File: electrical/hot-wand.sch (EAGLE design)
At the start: 184 parts, among them IC1 12V R-78K12-2.0, IC2 3V3 R-78K3.3, Q1 STP19NF20, Q2 IRF510, Q3 BC846B, Q4 SIRS5800DP-T1-GE3, Q5 2N7002K, Q6 DMTH64M2LPDWQ-13, Q7 G3404, SW1 SW-TACT-SIDE, U1 TPS54560DDA, U2 1EDN8511BXUSA1, U3 INA138, U4 LM74700QDBVTQ1, U5 AP53781, U6 SSD1306-4PIN-0.91N-VERT, U7 STM32F030F4P6, Y1 27.12 MHz 10pF

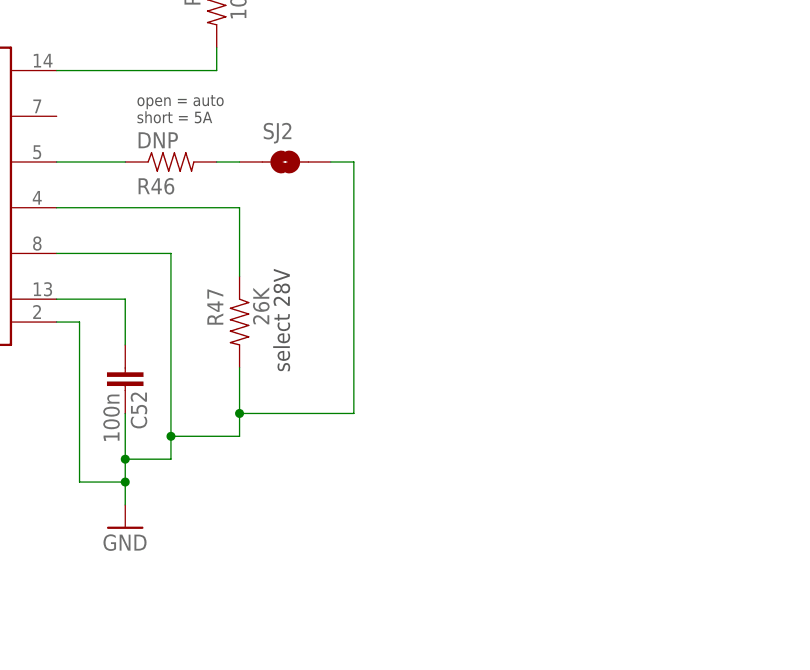
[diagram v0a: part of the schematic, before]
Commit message: added selectable voltage for USB
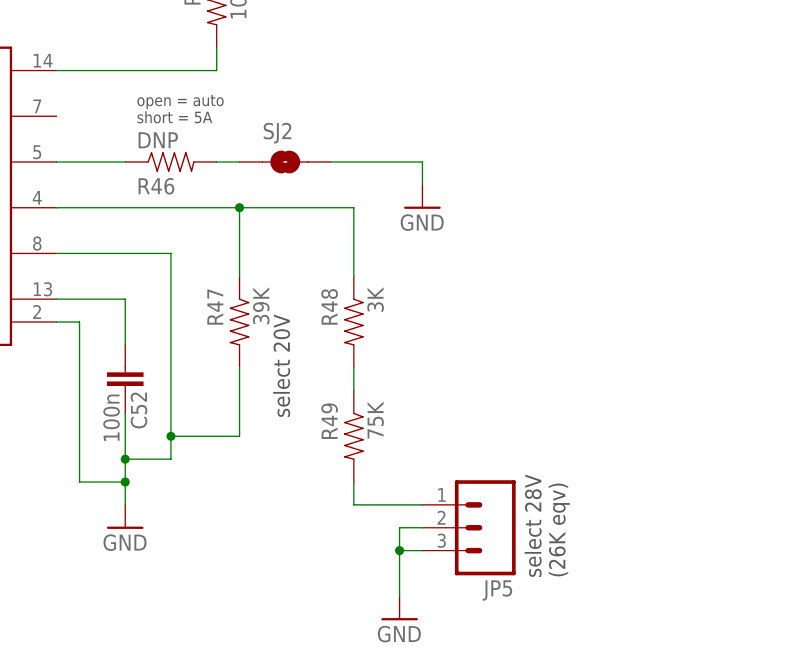
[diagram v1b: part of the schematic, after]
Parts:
- added JP5: (no value), hot-wand:M03LOCK
- added R48: 3K, hot-wand:RESISTOR0603-RES
- added R49: 75K, hot-wand:RESISTOR0603-RES
- R47: value 26K -> 39K; JLCPARTNUM C23356 -> C23153
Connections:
- new net N$60: R48.2, R49.1
- new net N$61: JP5.1, R49.2
- net GND: now also JP5.2, JP5.3
- net N$42: now also R48.1
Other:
- note added: "select 20V"
- note added: "select 28V (26K eqv)"
- note removed: "select 28V"
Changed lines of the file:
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@@
 </part>
 <part name="GND42" library="hot-wand" deviceset="GND" device=""/>
-<part name="R47" library="hot-wand" deviceset="RESISTOR" device="0603-RES" value="26K">
-<attribute name="JLCPARTNUM" value="C23356"/>
+<part name="R47" library="hot-wand" deviceset="RESISTOR" device="0603-RES" value="39K">
+<attribute name="JLCPARTNUM" value="C23153"/>
 </part>
 <part name="R34" library="hot-wand" deviceset="RESISTOR" device="0603-RES" value="4K7">
@@
 <part name="SJ6" library="hot-wand" deviceset="SJ-SMALL" device="-1206-SJ"/>
 <part name="SJ7" library="hot-wand" deviceset="SJ-SMALL" device="-1206-SJ"/>
+<part name="GND63" library="hot-wand" deviceset="GND" device=""/>
+<part name="R48" library="hot-wand" deviceset="RESISTOR" device="0603-RES" value="3K">
+<attribute name="JLCPARTNUM" value="C4211"/>
+</part>
+<part name="R49" library="hot-wand" deviceset="RESISTOR" device="0603-RES" value="75K">
+<attribute name="JLCPARTNUM" value="C23242"/>
+</part>
+<part name="JP5" library="hot-wand" deviceset="M03" device="LOCK"/>
+<part name="GND64" library="hot-wand" deviceset="GND" device=""/>
 </parts>
 <sheets>
@@
 0.11 Rdson</text>
 <text x="259.08" y="-251.46" size="1.016" layer="96" align="bottom-right">Bourns 5300-17-RC</text>
-<text x="156.21" y="-706.628" size="1.778" layer="97" rot="R270" align="bottom-right">select 28V</text>
+<text x="156.21" y="-711.708" size="1.778" layer="97" rot="R270" align="bottom-right">select 20V</text>
 <text x="58.42" y="-579.12" size="5.08" layer="97">XT-30 DC Input</text>
 <text x="25.4" y="-675.64" size="5.08" layer="97">USB-PD Input</text>
@@
 curr meas</text>
 <text x="251.46" y="-15.24" size="1.27" layer="97" align="top-left">actually about 20V</text>
+<text x="184.15" y="-729.488" size="1.778" layer="97" rot="R270" align="bottom-right">select 28V
+(26K eqv)</text>
 </plain>
 <instances>
@@
 <instance part="SJ6" gate="A" x="35.56" y="-223.52"/>
 <instance part="SJ7" gate="A" x="58.42" y="-182.88" rot="R90"/>
+<instance part="GND63" gate="1" x="172.72" y="-688.34"/>
+<instance part="R48" gate="G$1" x="165.1" y="-701.04" smashed="yes" rot="R270">
+<attribute name="NAME" x="161.5186" y="-697.23" size="1.778" layer="95" rot="R270"/>
+<attribute name="VALUE" x="166.624" y="-697.23" size="1.778" layer="96" rot="R270"/>
+<attribute name="JLCPARTNUM" x="165.1" y="-701.04" size="1.778" layer="96" rot="R270" display="off"/>
+</instance>
+<instance part="R49" gate="G$1" x="165.1" y="-713.74" smashed="yes" rot="R270">
+<attribute name="NAME" x="161.5186" y="-709.93" size="1.778" layer="95" rot="R270"/>
+<attribute name="VALUE" x="166.624" y="-709.93" size="1.778" layer="96" rot="R270"/>
+<attribute name="JLCPARTNUM" x="165.1" y="-713.74" size="1.778" layer="96" rot="R270" display="off"/>
+</instance>
+<instance part="JP5" gate="G$1" x="180.34" y="-723.9" rot="R180"/>
+<instance part="GND64" gate="1" x="170.18" y="-734.06"/>
 </instances>
 <busses>
@@
 <pinref part="R47" gate="G$1" pin="2"/>
 <wire x1="144.78" y1="-713.74" x2="152.4" y2="-713.74" width="0.1524" layer="91"/>
-<wire x1="152.4" y1="-713.74" x2="152.4" y2="-711.2" width="0.1524" layer="91"/>
 <junction x="144.78" y="-713.74"/>
 <junction x="139.7" y="-716.28"/>
 <junction x="139.7" y="-718.82"/>
-<wire x1="152.4" y1="-711.2" x2="152.4" y2="-706.12" width="0.1524" layer="91"/>
-<wire x1="152.4" y1="-711.2" x2="165.1" y2="-711.2" width="0.1524" layer="91"/>
-<wire x1="165.1" y1="-711.2" x2="165.1" y2="-683.26" width="0.1524" layer="91"/>
-<pinref part="SJ2" gate="1" pin="2"/>
-<wire x1="165.1" y1="-683.26" x2="162.56" y2="-683.26" width="0.1524" layer="91"/>
-<junction x="152.4" y="-711.2"/>
+<wire x1="152.4" y1="-713.74" x2="152.4" y2="-706.12" width="0.1524" layer="91"/>
 </segment>
 <segment>
@@
 <pinref part="GND62" gate="1" pin="GND"/>
 </segment>
+<segment>
+<pinref part="SJ2" gate="1" pin="2"/>
+<wire x1="172.72" y1="-683.26" x2="162.56" y2="-683.26" width="0.1524" layer="91"/>
+<pinref part="GND63" gate="1" pin="GND"/>
+<wire x1="172.72" y1="-685.8" x2="172.72" y2="-683.26" width="0.1524" layer="91"/>
+</segment>
+<segment>
+<pinref part="JP5" gate="G$1" pin="2"/>
+<pinref part="GND64" gate="1" pin="GND"/>
+<wire x1="172.72" y1="-723.9" x2="170.18" y2="-723.9" width="0.1524" layer="91"/>
+<wire x1="170.18" y1="-723.9" x2="170.18" y2="-726.44" width="0.1524" layer="91"/>
+<pinref part="JP5" gate="G$1" pin="3"/>
+<wire x1="170.18" y1="-726.44" x2="170.18" y2="-731.52" width="0.1524" layer="91"/>
+<wire x1="172.72" y1="-726.44" x2="170.18" y2="-726.44" width="0.1524" layer="91"/>
+<junction x="170.18" y="-726.44"/>
+</segment>
 </net>
 <net name="RF-OUT" class="0">
@@
 <wire x1="132.08" y1="-688.34" x2="152.4" y2="-688.34" width="0.1524" layer="91"/>
 <wire x1="152.4" y1="-688.34" x2="152.4" y2="-695.96" width="0.1524" layer="91"/>
+<pinref part="R48" gate="G$1" pin="1"/>
+<wire x1="152.4" y1="-688.34" x2="165.1" y2="-688.34" width="0.1524" layer="91"/>
+<wire x1="165.1" y1="-688.34" x2="165.1" y2="-695.96" width="0.1524" layer="91"/>
+<junction x="152.4" y="-688.34"/>
 </segment>
 </net>
@@
 </segment>
 </net>
+<net name="N$60" class="0">
+<segment>
+<pinref part="R48" gate="G$1" pin="2"/>
+<pinref part="R49" gate="G$1" pin="1"/>
+<wire x1="165.1" y1="-706.12" x2="165.1" y2="-708.66" width="0.1524" layer="91"/>
+</segment>
+</net>
+<net name="N$61" class="0">
+<segment>
+<pinref part="JP5" gate="G$1" pin="1"/>
+<pinref part="R49" gate="G$1" pin="2"/>
+<wire x1="172.72" y1="-721.36" x2="165.1" y2="-721.36" width="0.1524" layer="91"/>
+<wire x1="165.1" y1="-721.36" x2="165.1" y2="-718.82" width="0.1524" layer="91"/>
+</segment>
+</net>

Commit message: corrected a resistor part number
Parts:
- R30: JLCPARTNUM C2933230 -> C17667
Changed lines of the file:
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@@
 </part>
 <part name="R30" library="hot-wand" deviceset="RESISTOR" device="0603-RES" value="4K3">
-<attribute name="JLCPARTNUM" value="C2933230"/>
+<attribute name="JLCPARTNUM" value="C17667"/>
 </part>
 <part name="R31" library="hot-wand" deviceset="RESISTOR" device="0603-RES" value="100Ω">

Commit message: added a selector for ISEL
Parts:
- removed SJ7: SJ-SMALL-1206-SJ, hot-wand:SJ-SMALL-1206-SJ
- JP5: device hot-wand:M03LOCK -> hot-wand:M06LOCK
- R46: value DNP -> 0
- SJ5: value SOLDERJUMPERNO -> SJ-SMALL-1206-SJ; device hot-wand:SOLDERJUMPERNO -> hot-wand:SJ-SMALL-1206-SJ; JLC-DNP 1 -> (none)
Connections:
- net +12V: now also SJ5.1; no longer SJ6.1
- net BUCK-FB: now also SJ2.2; no longer SJ3.2
- net GND: now also JP5.5, JP5.6, SJ6.1; no longer SJ2.2, SJ7.1
- net N$50: now also SJ2.1; no longer SJ3.1
- net N$51: now also SJ3.1; no longer SJ5.1
- net N$55: now also JP5.1; no longer SJ2.1
- net N$58: now also SJ5.2; no longer SJ6.2
- net N$59: now also SJ6.2; no longer SJ7.2
- net N$61: now also JP5.4; no longer JP5.1
- net SWDIO: now also SJ3.2; no longer SJ5.2
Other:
- moved on the sheet: SJ2, SJ3, SJ6
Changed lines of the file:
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@@
 <attribute name="PARTNUM" value="TC33X-1-472E"/>
 </part>
-<part name="SJ3" library="hot-wand" deviceset="SOLDERJUMPER" device="NO" value="">
+<part name="SJ2" library="hot-wand" deviceset="SOLDERJUMPER" device="NO" value="">
 <attribute name="JLC-DNP" value="1"/>
 </part>
@@
 </part>
 <part name="GND59" library="hot-wand" deviceset="GND" device=""/>
-<part name="SJ5" library="hot-wand" deviceset="SOLDERJUMPER" device="NO" value="">
+<part name="SJ3" library="hot-wand" deviceset="SOLDERJUMPER" device="NO" value="">
 <attribute name="JLC-DNP" value="1"/>
 </part>
-<part name="R46" library="hot-wand" deviceset="RESISTOR" device="0603-RES" value="DNP">
-<attribute name="JLC-DNP" value="1"/>
-</part>
-<part name="SJ2" library="hot-wand" deviceset="SOLDERJUMPER" device="NO" value="">
+<part name="R46" library="hot-wand" deviceset="RESISTOR" device="0603-RES" value="0">
 <attribute name="JLC-DNP" value="1"/>
 </part>
@@
 <part name="GND1" library="hot-wand" deviceset="GND" device=""/>
 <part name="GND62" library="hot-wand" deviceset="GND" device=""/>
+<part name="SJ5" library="hot-wand" deviceset="SJ-SMALL" device="-1206-SJ"/>
 <part name="SJ6" library="hot-wand" deviceset="SJ-SMALL" device="-1206-SJ"/>
-<part name="SJ7" library="hot-wand" deviceset="SJ-SMALL" device="-1206-SJ"/>
-<part name="GND63" library="hot-wand" deviceset="GND" device=""/>
 <part name="R48" library="hot-wand" deviceset="RESISTOR" device="0603-RES" value="3K">
 <attribute name="JLCPARTNUM" value="C4211"/>
@@
 <attribute name="JLCPARTNUM" value="C23242"/>
 </part>
-<part name="JP5" library="hot-wand" deviceset="M03" device="LOCK"/>
 <part name="GND64" library="hot-wand" deviceset="GND" device=""/>
+<part name="JP5" library="hot-wand" deviceset="M06" device="LOCK"/>
 </parts>
 <sheets>
@@
 curr meas</text>
 <text x="251.46" y="-15.24" size="1.27" layer="97" align="top-left">actually about 20V</text>
-<text x="184.15" y="-729.488" size="1.778" layer="97" rot="R270" align="bottom-right">select 28V
+<text x="173.99" y="-726.948" size="1.778" layer="97" rot="R270" align="bottom-right">select 28V
 (26K eqv)</text>
 </plain>
@@
 <attribute name="VALUE" x="341.376" y="-183.134" size="1.778" layer="95" rot="R90"/>
 </instance>
-<instance part="SJ3" gate="1" x="358.14" y="-177.8" rot="R90"/>
+<instance part="SJ2" gate="1" x="358.14" y="-177.8" rot="R90"/>
 <instance part="R42" gate="G$1" x="233.68" y="-431.8" rot="R90"/>
 <instance part="R43" gate="G$1" x="259.08" y="-431.8" rot="R90"/>
@@
 </instance>
 <instance part="GND59" gate="1" x="304.8" y="-462.28"/>
-<instance part="SJ5" gate="1" x="297.18" y="-444.5" rot="R180"/>
+<instance part="SJ3" gate="1" x="297.18" y="-444.5" rot="R180"/>
 <instance part="R46" gate="G$1" x="144.78" y="-683.26" smashed="yes">
 <attribute name="NAME" x="140.97" y="-686.8414" size="1.778" layer="95"/>
 <attribute name="VALUE" x="140.97" y="-681.736" size="1.778" layer="96"/>
 </instance>
-<instance part="SJ2" gate="1" x="157.48" y="-683.26"/>
 <instance part="VR3" gate="G$1" x="297.18" y="-264.16" smashed="yes" rot="R90">
 <attribute name="NAME" x="296.418" y="-259.08" size="1.778" layer="95" rot="R180"/>
@@
 </instance>
 <instance part="GND62" gate="1" x="299.72" y="-421.64"/>
-<instance part="SJ6" gate="A" x="35.56" y="-223.52"/>
-<instance part="SJ7" gate="A" x="58.42" y="-182.88" rot="R90"/>
-<instance part="GND63" gate="1" x="172.72" y="-688.34"/>
+<instance part="SJ5" gate="A" x="35.56" y="-223.52"/>
+<instance part="SJ6" gate="A" x="58.42" y="-182.88" rot="R90"/>
 <instance part="R48" gate="G$1" x="165.1" y="-701.04" smashed="yes" rot="R270">
 <attribute name="NAME" x="161.5186" y="-697.23" size="1.778" layer="95" rot="R270"/>
@@
 <attribute name="JLCPARTNUM" x="165.1" y="-713.74" size="1.778" layer="96" rot="R270" display="off"/>
 </instance>
-<instance part="JP5" gate="G$1" x="180.34" y="-723.9" rot="R180"/>
-<instance part="GND64" gate="1" x="170.18" y="-734.06"/>
+<instance part="GND64" gate="1" x="180.34" y="-703.58"/>
+<instance part="JP5" gate="G$1" x="187.96" y="-688.34" rot="R180"/>
 </instances>
 <busses>
@@
 <junction x="33.02" y="-193.04"/>
 <junction x="58.42" y="-193.04"/>
-<pinref part="SJ7" gate="A" pin="1"/>
+<pinref part="SJ6" gate="A" pin="1"/>
 <wire x1="58.42" y1="-185.42" x2="58.42" y2="-193.04" width="0.1524" layer="91"/>
 </segment>
@@
 </segment>
 <segment>
-<pinref part="SJ2" gate="1" pin="2"/>
-<wire x1="172.72" y1="-683.26" x2="162.56" y2="-683.26" width="0.1524" layer="91"/>
-<pinref part="GND63" gate="1" pin="GND"/>
-<wire x1="172.72" y1="-685.8" x2="172.72" y2="-683.26" width="0.1524" layer="91"/>
-</segment>
-<segment>
 <pinref part="JP5" gate="G$1" pin="2"/>
 <pinref part="GND64" gate="1" pin="GND"/>
-<wire x1="172.72" y1="-723.9" x2="170.18" y2="-723.9" width="0.1524" layer="91"/>
-<wire x1="170.18" y1="-723.9" x2="170.18" y2="-726.44" width="0.1524" layer="91"/>
+<wire x1="182.88" y1="-685.8" x2="180.34" y2="-685.8" width="0.1524" layer="91"/>
+<wire x1="180.34" y1="-685.8" x2="180.34" y2="-688.34" width="0.1524" layer="91"/>
 <pinref part="JP5" gate="G$1" pin="3"/>
-<wire x1="170.18" y1="-726.44" x2="170.18" y2="-731.52" width="0.1524" layer="91"/>
-<wire x1="172.72" y1="-726.44" x2="170.18" y2="-726.44" width="0.1524" layer="91"/>
-<junction x="170.18" y="-726.44"/>
+<wire x1="180.34" y1="-688.34" x2="180.34" y2="-693.42" width="0.1524" layer="91"/>
+<wire x1="180.34" y1="-693.42" x2="180.34" y2="-695.96" width="0.1524" layer="91"/>
+<wire x1="180.34" y1="-695.96" x2="180.34" y2="-701.04" width="0.1524" layer="91"/>
+<wire x1="182.88" y1="-688.34" x2="180.34" y2="-688.34" width="0.1524" layer="91"/>
+<pinref part="JP5" gate="G$1" pin="5"/>
+<wire x1="182.88" y1="-693.42" x2="180.34" y2="-693.42" width="0.1524" layer="91"/>
+<pinref part="JP5" gate="G$1" pin="6"/>
+<wire x1="182.88" y1="-695.96" x2="180.34" y2="-695.96" width="0.1524" layer="91"/>
+<junction x="180.34" y="-695.96"/>
+<junction x="180.34" y="-693.42"/>
+<junction x="180.34" y="-688.34"/>
 </segment>
 </net>
@@
 <pinref part="P+3" gate="1" pin="+12V"/>
 <wire x1="25.4" y1="-223.52" x2="25.4" y2="-220.98" width="0.1524" layer="91"/>
-<pinref part="SJ6" gate="A" pin="1"/>
+<pinref part="SJ5" gate="A" pin="1"/>
 <wire x1="33.02" y1="-223.52" x2="25.4" y2="-223.52" width="0.1524" layer="91"/>
 </segment>
@@
 <label x="370.84" y="-165.1" size="1.778" layer="95" xref="yes"/>
 <wire x1="355.6" y1="-165.1" x2="358.14" y2="-165.1" width="0.1524" layer="91"/>
-<pinref part="SJ3" gate="1" pin="2"/>
+<pinref part="SJ2" gate="1" pin="2"/>
 <wire x1="358.14" y1="-165.1" x2="370.84" y2="-165.1" width="0.1524" layer="91"/>
 <wire x1="358.14" y1="-172.72" x2="358.14" y2="-165.1" width="0.1524" layer="91"/>
@@
 </segment>
 <segment>
-<pinref part="SJ5" gate="1" pin="2"/>
+<pinref part="SJ3" gate="1" pin="2"/>
 <wire x1="292.1" y1="-444.5" x2="289.56" y2="-444.5" width="0.1524" layer="91"/>
 <label x="289.56" y="-444.5" size="1.778" layer="95" rot="R180" xref="yes"/>
@@
 <wire x1="342.9" y1="-193.04" x2="342.9" y2="-195.58" width="0.1524" layer="91"/>
 <wire x1="342.9" y1="-195.58" x2="350.52" y2="-195.58" width="0.1524" layer="91"/>
-<pinref part="SJ3" gate="1" pin="1"/>
+<pinref part="SJ2" gate="1" pin="1"/>
 <wire x1="350.52" y1="-185.42" x2="358.14" y2="-185.42" width="0.1524" layer="91"/>
 <wire x1="358.14" y1="-185.42" x2="358.14" y2="-182.88" width="0.1524" layer="91"/>
@@
 <pinref part="R44" gate="G$1" pin="1"/>
 <wire x1="304.8" y1="-447.04" x2="304.8" y2="-444.5" width="0.1524" layer="91"/>
-<pinref part="SJ5" gate="1" pin="1"/>
+<pinref part="SJ3" gate="1" pin="1"/>
 <wire x1="304.8" y1="-444.5" x2="302.26" y2="-444.5" width="0.1524" layer="91"/>
 <pinref part="R45" gate="G$1" pin="1"/>
@@
 <segment>
 <pinref part="R46" gate="G$1" pin="2"/>
-<pinref part="SJ2" gate="1" pin="1"/>
-<wire x1="149.86" y1="-683.26" x2="152.4" y2="-683.26" width="0.1524" layer="91"/>
+<wire x1="182.88" y1="-683.26" x2="149.86" y2="-683.26" width="0.1524" layer="91"/>
+<pinref part="JP5" gate="G$1" pin="1"/>
 </segment>
 </net>
@@
 <junction x="40.64" y="-223.52"/>
 <junction x="55.88" y="-223.52"/>
-<pinref part="SJ6" gate="A" pin="2"/>
+<pinref part="SJ5" gate="A" pin="2"/>
 </segment>
 </net>
@@
 <pinref part="Q1" gate="G$1" pin="S"/>
 <wire x1="58.42" y1="-180.34" x2="58.42" y2="-177.8" width="0.1524" layer="91"/>
-<pinref part="SJ7" gate="A" pin="2"/>
+<pinref part="SJ6" gate="A" pin="2"/>
 </segment>
 </net>
@@
 <net name="N$61" class="0">
 <segment>
-<pinref part="JP5" gate="G$1" pin="1"/>
 <pinref part="R49" gate="G$1" pin="2"/>
 <wire x1="172.72" y1="-721.36" x2="165.1" y2="-721.36" width="0.1524" layer="91"/>
 <wire x1="165.1" y1="-721.36" x2="165.1" y2="-718.82" width="0.1524" layer="91"/>
-</segment>
-</net>
+<wire x1="172.72" y1="-721.36" x2="172.72" y2="-690.88" width="0.1524" layer="91"/>
+<pinref part="JP5" gate="G$1" pin="4"/>
+<wire x1="172.72" y1="-690.88" x2="179.832" y2="-690.88" width="0.1524" layer="91"/>
+<wire x1="180.848" y1="-690.88" x2="182.88" y2="-690.88" width="0.1524" layer="91"/>
+<wire x1="179.832" y1="-690.88" x2="180.848" y2="-690.88" width="0.1524" layer="91" curve="-180"/>
+</segment>
+</net>

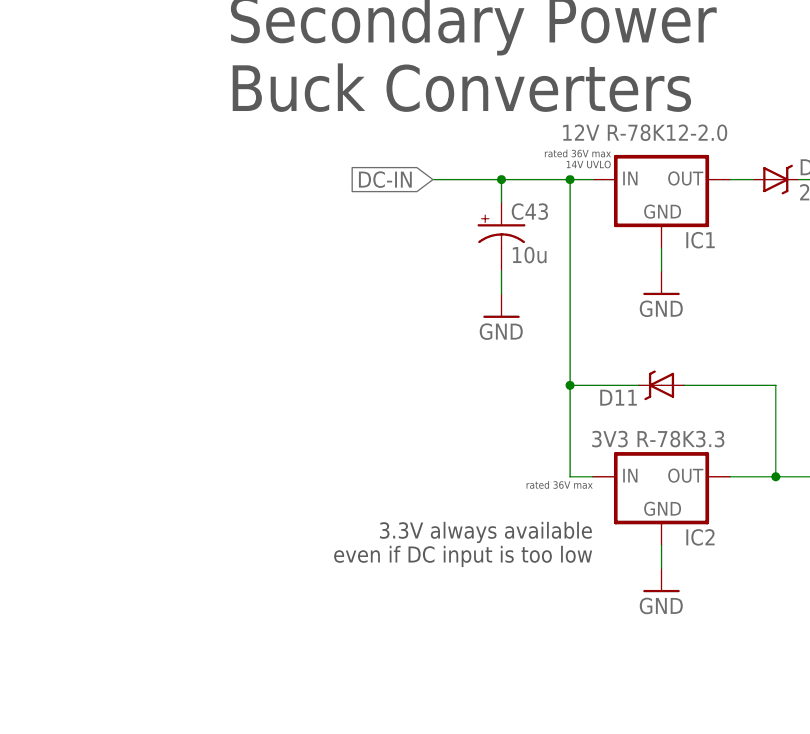
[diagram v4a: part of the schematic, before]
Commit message: added an option to use 3.3V regulator from 12V
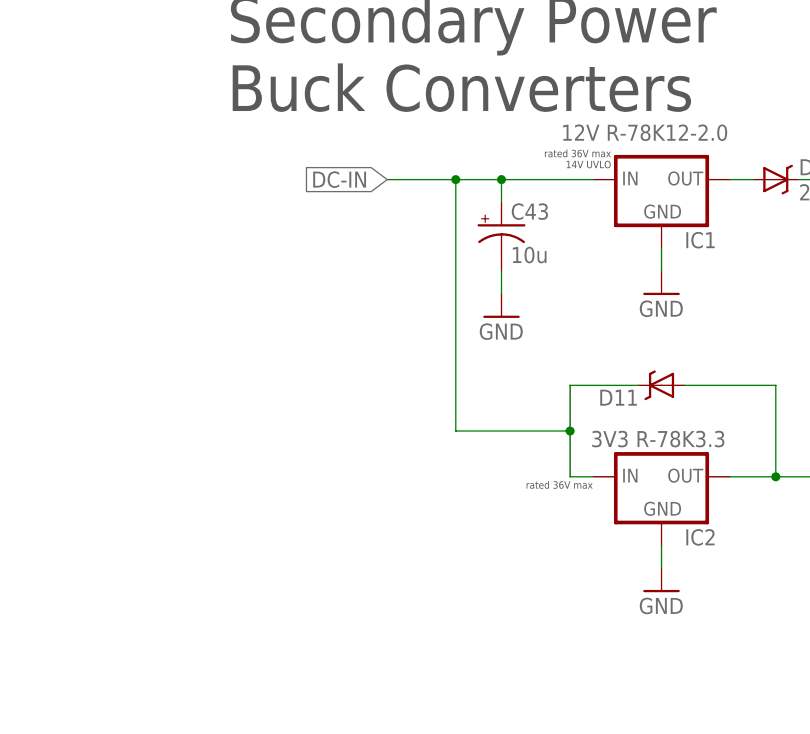
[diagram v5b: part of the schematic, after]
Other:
- note removed: "3.3V always available even if DC input is too low"
